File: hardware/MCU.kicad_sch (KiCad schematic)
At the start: 12 parts, among them SW1 MCP_HW_ADDR_SEL, SW2 MCP_N_RST, U1 MCP23017_SO

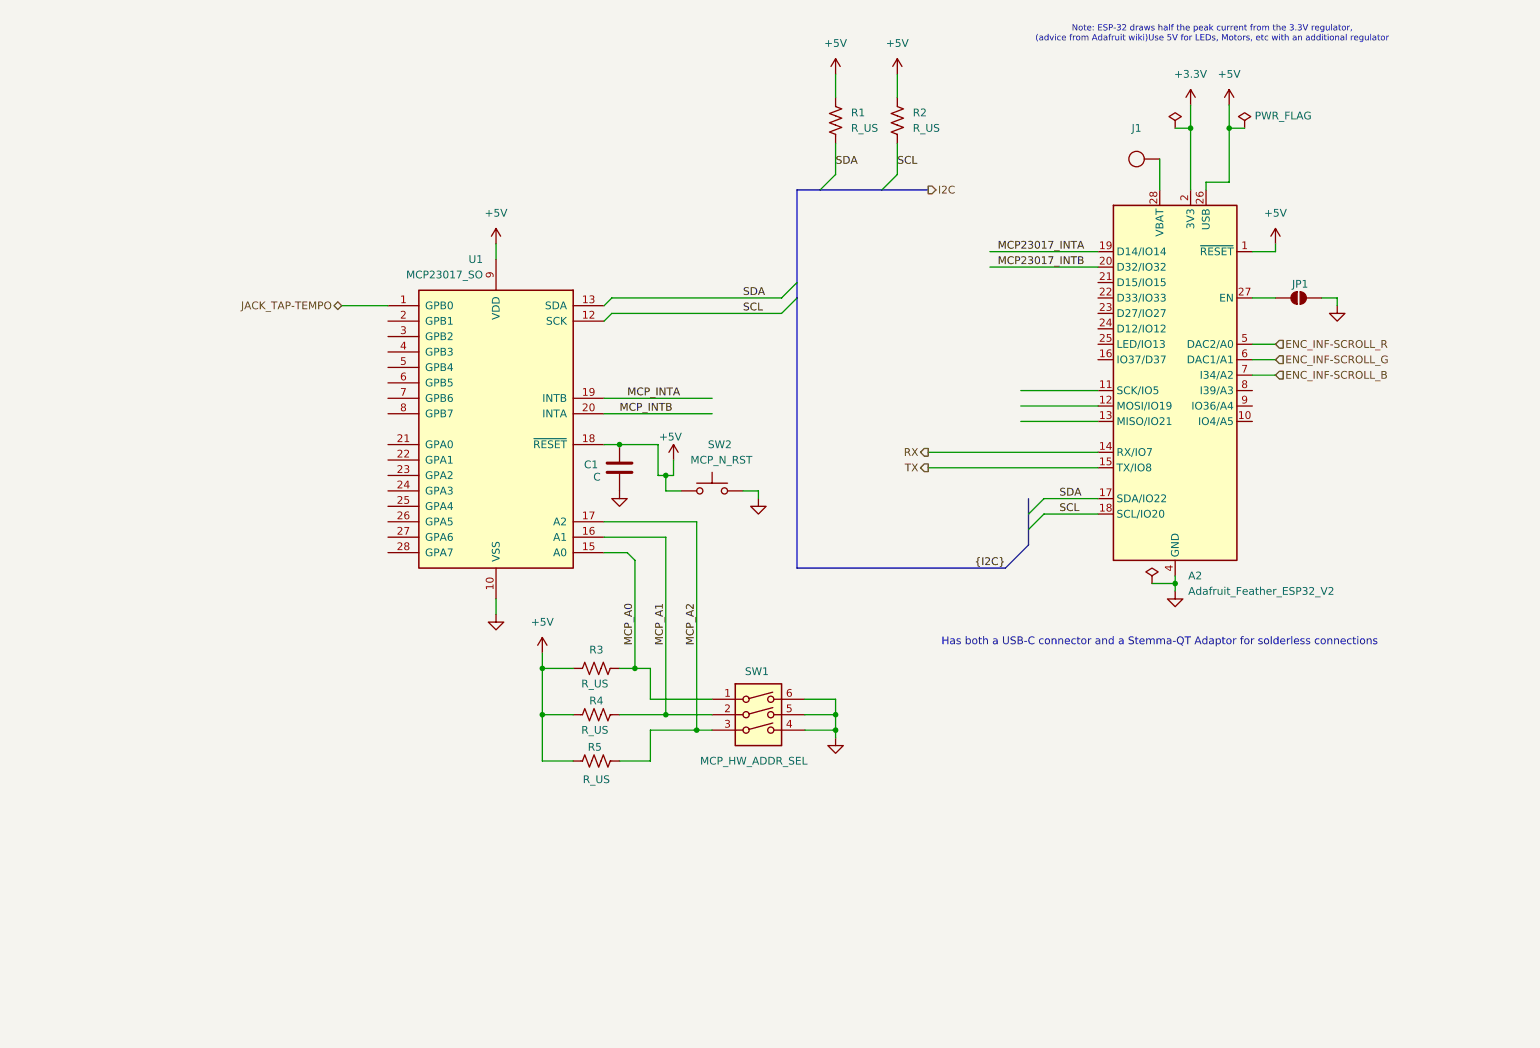
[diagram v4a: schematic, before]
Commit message: feat: Connected main HW UI components to MCU
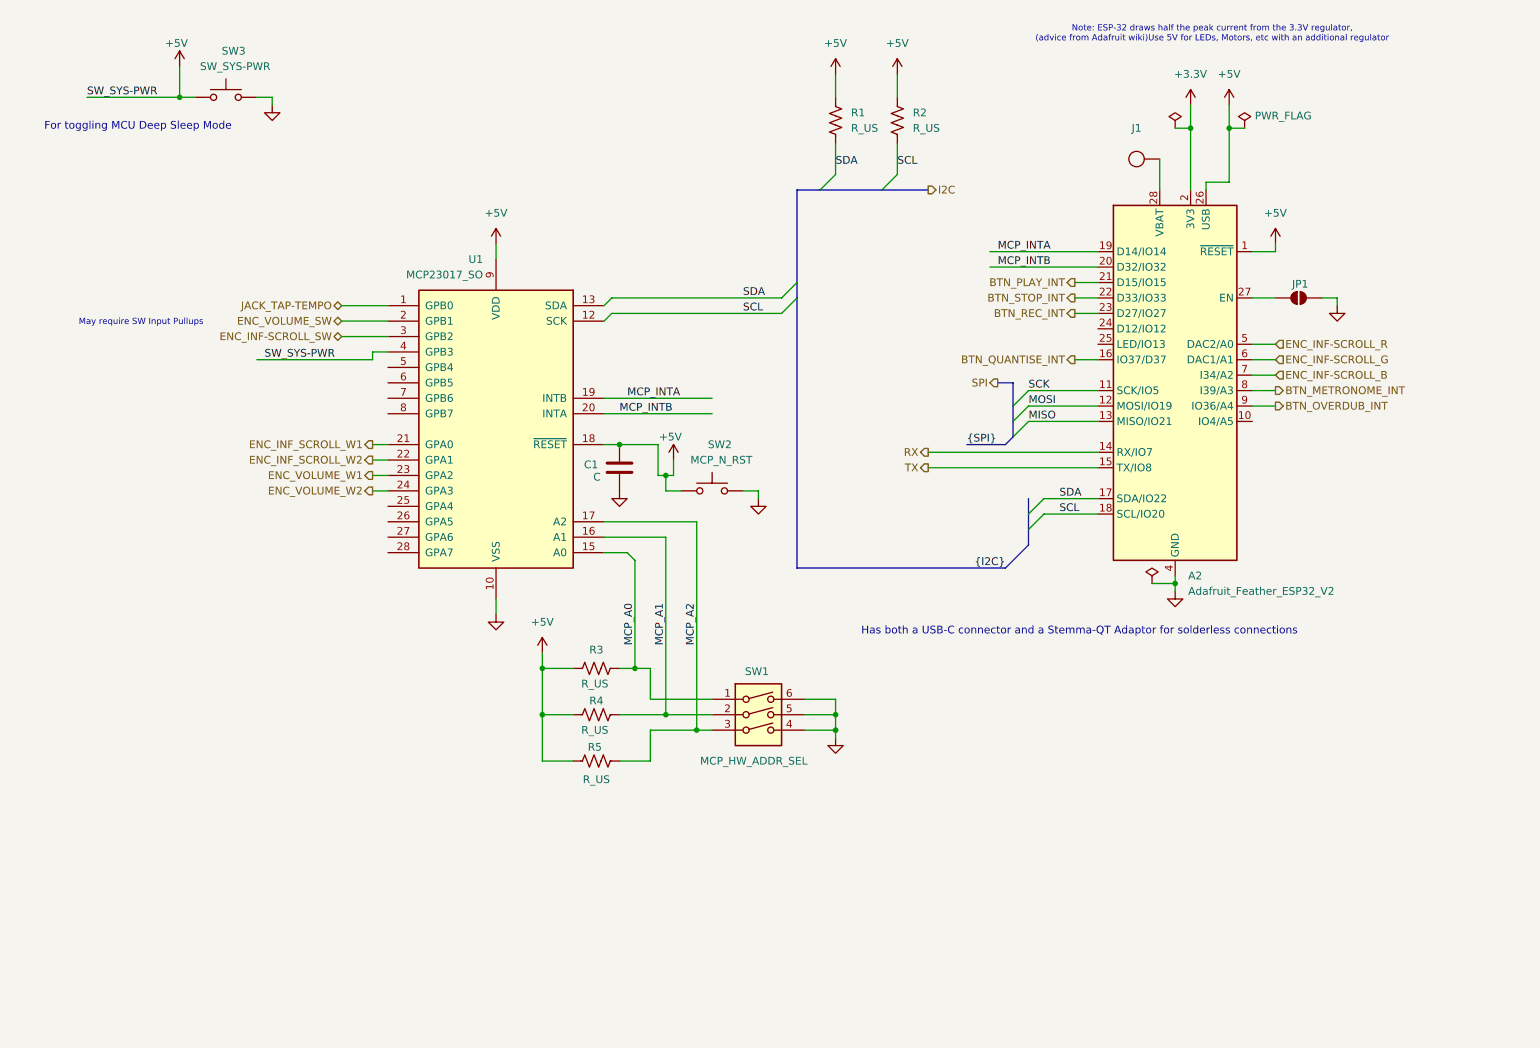
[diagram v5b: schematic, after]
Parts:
- added SW3: SW_SYS-PWR, symbol Switch:SW_Push
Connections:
- net MCP23017_INTA is gone; now on net MCP_INTA: A2.19 (D14/IO14)
- net MCP23017_INTB is gone; now on net MCP_INTB: A2.20 (D32/IO32)
- net +5V: now also U1.4 (GPB3), SW3.1
- net GND: now also SW3.2
- net SCK: now reaches A2.11 (SCK/IO5)
- net MOSI: now reaches A2.12 (MOSI/IO19)
- net MISO: now reaches A2.13 (MISO/IO21)
- net BTN_QUANTISE_INT: now reaches A2.16 (IO37/D37)
- net BTN_PLAY_INT: now reaches A2.21 (D15/IO15)
- net BTN_STOP_INT: now reaches A2.22 (D33/IO33)
- net BTN_REC_INT: now reaches A2.23 (D27/IO27)
- net BTN_METRONOME_INT: now reaches A2.8 (I39/A3)
- net BTN_OVERDUB_INT: now reaches A2.9 (IO36/A4)
- net ENC_VOLUME_SW: now reaches U1.2 (GPB1)
- net ENC_INF_SCROLL_W1: now reaches U1.21 (GPA0)
- net ENC_INF_SCROLL_W2: now reaches U1.22 (GPA1)
- net ENC_VOLUME_W1: now reaches U1.23 (GPA2)
- net ENC_VOLUME_W2: now reaches U1.24 (GPA3)
- net ENC_INF-SCROLL_SW: now reaches U1.3 (GPB2)
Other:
- note added: "For toggling MCU Deep Sleep Mode"
- note added: "May require SW Input Pullups"

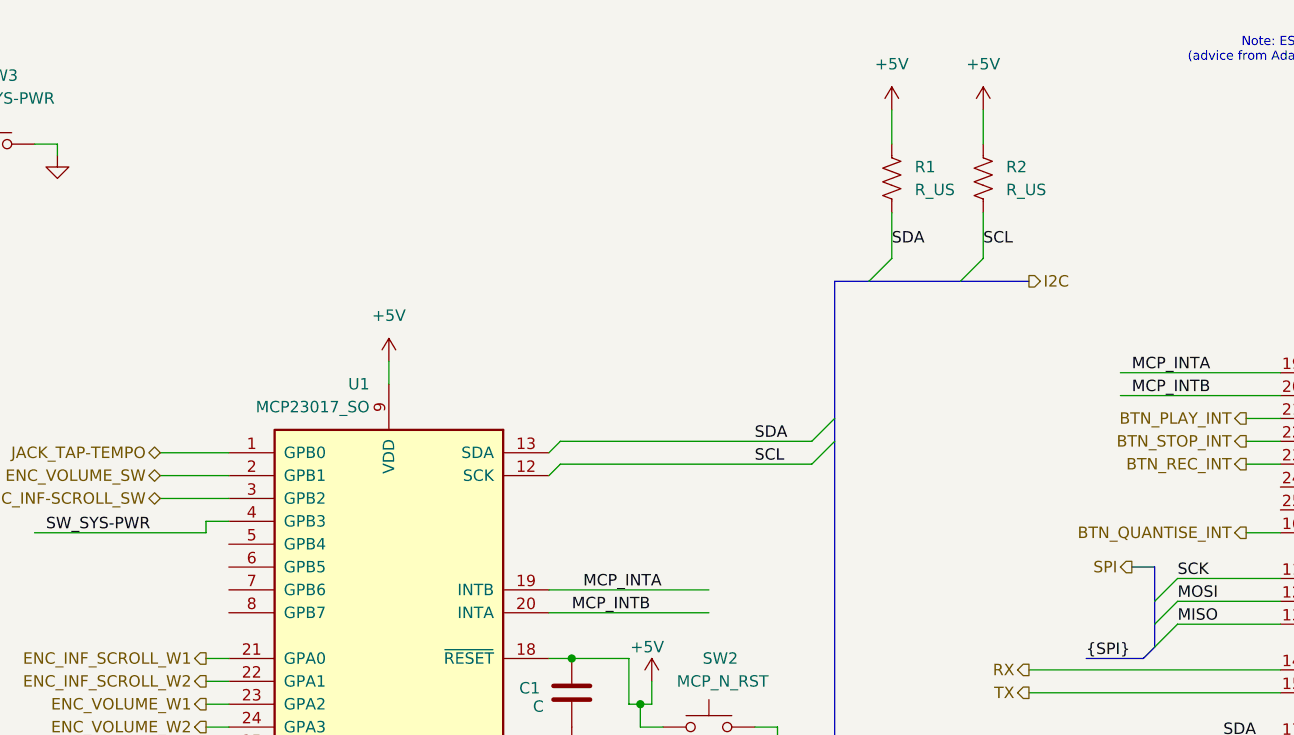
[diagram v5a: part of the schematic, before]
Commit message: feat [HWE}; Added SPI Oled and refactor DuPPa LED
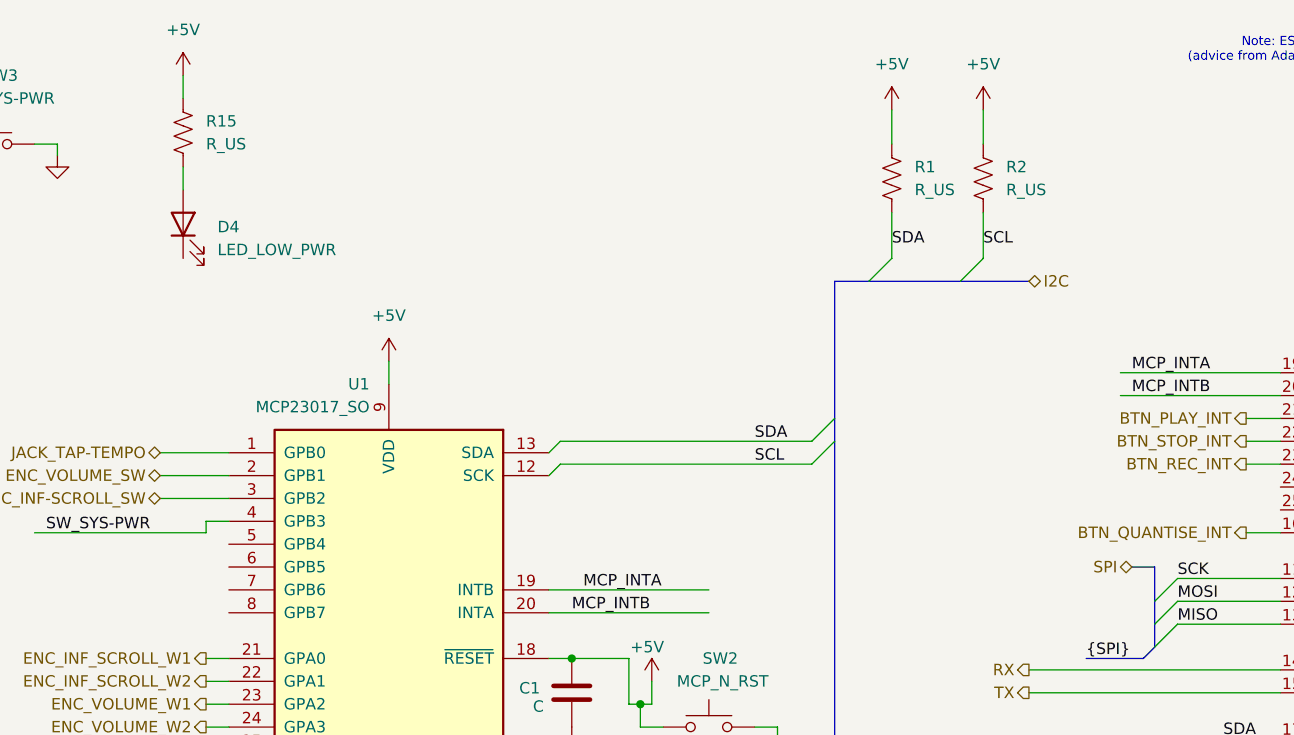
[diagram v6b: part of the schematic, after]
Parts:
- added D4: LED_LOW_PWR, symbol Device:LED
- added R15: R_US, symbol Device:R_US
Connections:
- net +5V: now also R15.1
- new net: D4.2 (A), R15.2
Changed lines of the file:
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@@
+	(wire
+		(pts
+			(xy 71.12 30.48) (xy 71.12 33.02)
+		)
+		(stroke
+			(width 0)
+			(type default)
+		)
+	)
 	(wire
 		(pts
@@
 		(pts
 			(xy 214.63 33.02) (xy 214.63 41.91)
+		)
+		(stroke
+			(width 0)
+			(type default)
+		)
+	)
+	(wire
+		(pts
+			(xy 71.12 20.32) (xy 71.12 22.86)
 		)
 		(stroke
@@
 	)
 	(hierarchical_label "SPI"
-		(shape output)
+		(shape bidirectional)
 		(at 176.53 74.93 180)
 		(effects
@@
 	)
 	(hierarchical_label "I2C"
-		(shape output)
+		(shape bidirectional)
 		(at 165.1 43.18 0)
 		(effects
@@
 	)
 	(symbol
+		(lib_id "4ms_Power-symbol:+5V")
+		(at 71.12 20.32 0)
+		(unit 1)
+		(exclude_from_sim no)
+		(in_bom yes)
+		(on_board yes)
+		(dnp no)
+		(fields_autoplaced yes)
+		(property "Reference" "#PWR047"
+			(at 71.12 24.13 0)
+			(effects
+				(font
+					(size 1.27 1.27)
+				)
+				(hide yes)
+			)
+		)
+		(property "Value" "+5V"
+			(at 71.12 15.24 0)
+			(effects
+				(font
+					(size 1.27 1.27)
+				)
+			)
+		)
+		(property "Footprint" ""
+			(at 71.12 20.32 0)
+			(effects
+				(font
+					(size 1.27 1.27)
+				)
+				(hide yes)
+			)
+		)
+		(property "Datasheet" ""
+			(at 71.12 20.32 0)
+			(effects
+				(font
+					(size 1.27 1.27)
+				)
+				(hide yes)
+			)
+		)
+		(property "Description" ""
+			(at 71.12 20.32 0)
+			(effects
+				(font
+					(size 1.27 1.27)
+				)
+				(hide yes)
+			)
+		)
+		(pin "1"
+		)
+		(instances
+			(project "10032025_01_[HWE] Simple Transport Midi Controller"
+				(path "/4f4cdf46-015d-4b38-9cc1-de7a767260f6/701e2ee7-1555-4be3-8e0c-a769d2df25b2"
+					(reference "#PWR047")
+					(unit 1)
+				)
+			)
+		)
+	)
+	(symbol
 		(lib_id "power:PWR_FLAG")
 		(at 205.74 33.02 0)
@@
 				(path "/4f4cdf46-015d-4b38-9cc1-de7a767260f6/701e2ee7-1555-4be3-8e0c-a769d2df25b2"
 					(reference "SW1")
+					(unit 1)
+				)
+			)
+		)
+	)
+	(symbol
+		(lib_id "Device:R_US")
+		(at 71.12 26.67 0)
+		(unit 1)
+		(exclude_from_sim no)
+		(in_bom yes)
+		(on_board yes)
+		(dnp no)
+		(fields_autoplaced yes)
+		(property "Reference" "R15"
+			(at 73.66 25.3999 0)
+			(effects
+				(font
+					(size 1.27 1.27)
+				)
+				(justify left)
+			)
+		)
+		(property "Value" "R_US"
+			(at 73.66 27.9399 0)
+			(effects
+				(font
+					(size 1.27 1.27)
+				)
+				(justify left)
+			)
+		)
+		(property "Footprint" ""
+			(at 72.136 26.924 90)
+			(effects
+				(font
+					(size 1.27 1.27)
+				)
+				(hide yes)
+			)
+		)
+		(property "Datasheet" "~"
+			(at 71.12 26.67 0)
+			(effects
+				(font
+					(size 1.27 1.27)
+				)
+				(hide yes)
+			)
+		)
+		(property "Description" "Resistor, US symbol"
+			(at 71.12 26.67 0)
+			(effects
+				(font
+					(size 1.27 1.27)
+				)
+				(hide yes)
+			)
+		)
+		(pin "2"
+		)
+		(pin "1"
+		)
+		(instances
+			(project "10032025_01_[HWE] Simple Transport Midi Controller"
+				(path "/4f4cdf46-015d-4b38-9cc1-de7a767260f6/701e2ee7-1555-4be3-8e0c-a769d2df25b2"
+					(reference "R15")
 					(unit 1)
 				)
@@
 					(unit 1)
 				)
+			)
+		)
+	)
+	(symbol
+		(lib_id "Device:LED")
+		(at 71.12 36.83 90)
+		(unit 1)
+		(exclude_from_sim no)
+		(in_bom yes)
+		(on_board yes)
+		(dnp no)
+		(fields_autoplaced yes)
+		(property "Reference" "D4"
+			(at 74.93 37.1474 90)
+			(effects
+				(font
+					(size 1.27 1.27)
+				)
+				(justify right)
+			)
+		)
+		(property "Value" "LED_LOW_PWR"
+			(at 74.93 39.6874 90)
+			(effects
+				(font
+					(size 1.27 1.27)
+				)
+				(justify right)
+			)
+		)
+		(property "Footprint" ""
+			(at 71.12 36.83 0)
+			(effects
+				(font
+					(size 1.27 1.27)
+				)
+				(hide yes)
+			)
+		)
+		(property "Datasheet" "~"
+			(at 71.12 36.83 0)
+			(effects
+				(font
+					(size 1.27 1.27)
+				)
+				(hide yes)
+			)
+		)
+		(property "Description" "Light emitting diode"
+			(at 71.12 36.83 0)
+			(effects
+				(font
+					(size 1.27 1.27)
+				)
+				(hide yes)
+			)
+		)
+		(property "Sim.Pins" "1=K 2=A"
+			(at 71.12 36.83 0)
+			(effects
+				(font
+					(size 1.27 1.27)
+				)
+				(hide yes)
+			)
+		)
+		(pin "2"
+		)
+		(pin "1"
+		)
+		(instances
+			(project "10032025_01_[HWE] Simple Transport Midi Controller"
+				(path "/4f4cdf46-015d-4b38-9cc1-de7a767260f6/701e2ee7-1555-4be3-8e0c-a769d2df25b2"
+					(reference "D4")
+					(unit 1)
+				)
